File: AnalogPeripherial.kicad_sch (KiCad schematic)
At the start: 52 parts, among them J1 USART, J2 SWD, J3 USB_B_Mini, SW1 record, SW2 replay, SW3 SW_Nidec_CAS-120A1, U1 LD1117S33TR_SOT223, U2 STM32F373CCTx, U3 LM386, U5 TLV9061xDBV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

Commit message: PCB design still in progress
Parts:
- added C23: 33p, Capacitor_SMD:C_0805_2012Metric_Pad1.18x1.45mm_HandSolder, symbol Device:C
- added C24: 10u, Capacitor_SMD:C_0805_2012Metric_Pad1.18x1.45mm_HandSolder, symbol Device:C
- C16: value 100p -> 100u
- C17: value 0.047u -> 0.05u
- C18: value 470u -> 250u
- C19: value 330n -> 68n
- C20: value 47u -> 40u
- C21: value 120p -> 995p
- C22: value 3.3u -> 150n
- R11: value 10k -> 100
- R6: value 5.9k -> 2.2k
- R7, R8: value 200k -> 100k
- R9: value 787 -> 78.7
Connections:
- net 3V3: now also U2.1 (VBAT), U2.17 (VDD), U2.48 (VDD)
- net 3VA3: now also U2.24 (VDDSD), U2.9 (VDDA)
- net ADC1_IN1: now also R11.1; no longer R11.2
- net DAC1_OUT1: now also C24.1; no longer RV1.1
- net GND: now also C22.1, C23.1; no longer R11.1, U2.1 (VBAT), U2.17 (VDD), U2.24 (VDDSD), U2.48 (VDD), U2.9 (VDDA)
- net SPI1_NSS: now also U2.21 (PE8); no longer U2.38 (PA15)
- net at C21.2, R10.2, U5.1: now also R11.2; no longer C22.1
- net at C19.1, MK1.2 (+), R6.2: now also C23.2
- net NRST: no longer names the net of C1.1, U2.7 (NRST)
- new net: C24.2, RV1.1
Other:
- moved on the sheet: C1, C11, C12, C13, C14, C2, C4, C5, C7, C8, C9, D1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

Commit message: Finished model of PCB
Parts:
- removed U4: ~, my_custom_stuff:microSD, symbol my_custom_stuff:microSD
- added H1, H2, H3, H4: MountingHole, MountingHole:MountingHole_2.2mm_M2, symbol Mechanical:MountingHole
- added U4: ~, project:microSD, symbol project:SD_Card
- SW1, SW2: footprint my_custom_stuff:button -> project:button
- U3: footprint ADL5370ACPZ:M08A_TEX -> Package_SO:PowerIntegrations_SO-8
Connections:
- net 3V3: now also U4.4 (VDD); no longer R6.1, R7.1, U5.5 (V+)
- net 3VA3: now also R6.1, R7.1, U5.5 (V+)
- net GND: now also J3.6 (Shield), U4.12 (GND), U4.13 (GND), U4.14 (GND), U4.15 (GND), U4.6 (VSS)
- net PUSH_REC: now also U2.3 (PC14); no longer U2.19 (PB1)
- net PUSH_REPLAY: now also U2.2 (PC13); no longer U2.20 (PB2)
- net SPI1_MISO: now also U4.7 (DAT0)
- net SPI1_MOSI: now also U4.3 (CMD)
- net SPI1_NSS: now also U4.2 (CD)
- net SPI1_SCK: now also U4.5 (CLK)
- net SWCLK: now also J2.2 (Pin_2); no longer J2.3 (Pin_3)
- net SWDIO: now also J2.3 (Pin_3); no longer J2.2 (Pin_2)
- no-connect marks 26 -> 25
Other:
- moved on the sheet: C15, C16, C17, C18, C24, D2, D3, J1, J2, LS1, R3, R4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

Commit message: Order all files and folders
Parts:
- C18: value 250u -> 100u
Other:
- note added: "additional"
- note added: "ideally 250u"
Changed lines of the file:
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@@
 		)
 	)
+	(text "additional\n"
+		(exclude_from_sim no)
+		(at 221.488 123.952 0)
+		(effects
+			(font
+				(size 1.27 1.27)
+			)
+		)
+	)
 	(text "Power supply"
 		(exclude_from_sim no)
@@
 		)
 	)
+	(text "ideally 250u\n"
+		(exclude_from_sim no)
+		(at 247.396 92.456 0)
+		(effects
+			(font
+				(size 1.27 1.27)
+			)
+		)
+	)
 	(global_label "SWCLK"
 		(shape input)
@@
 		)
 		(instances
-			(project ""
+			(project "AnalogPeripherial"
 				(path "/0b175dd1-a91a-485c-9ff0-418ddbedb12c"
 					(reference "H1")
@@
 			)
 		)
-		(property "Value" "250u"
+		(property "Value" "100u"
 			(at 247.65 97.79 90)
 			(effects
@@
 		)
 		(instances
-			(project ""
+			(project "AnalogPeripherial"
 				(path "/0b175dd1-a91a-485c-9ff0-418ddbedb12c"
 					(reference "U4")

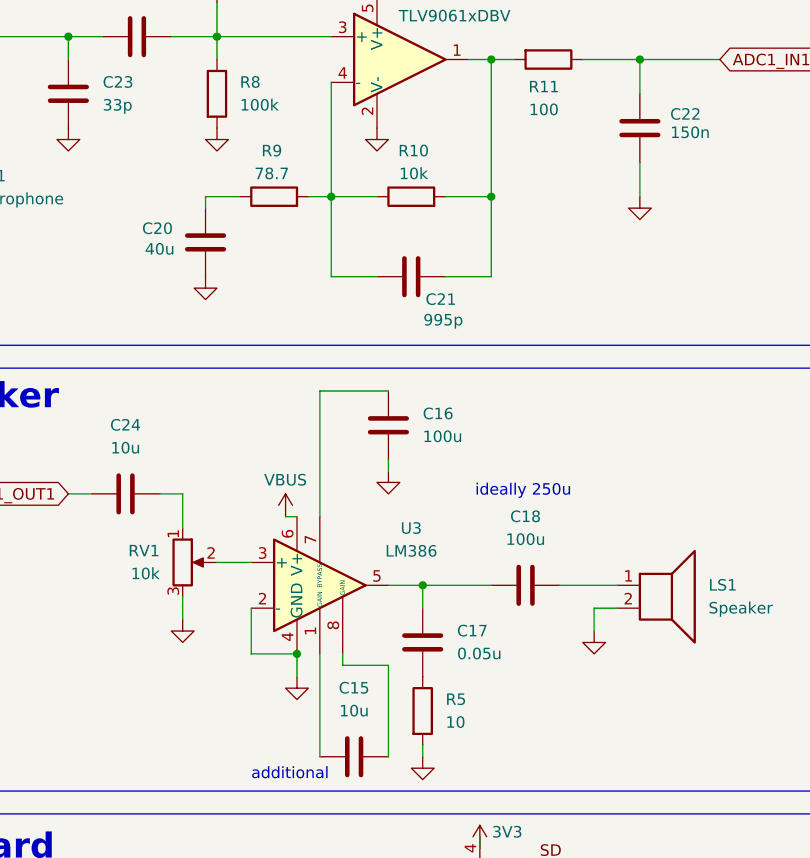
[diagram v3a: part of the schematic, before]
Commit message: Small changes in values of components
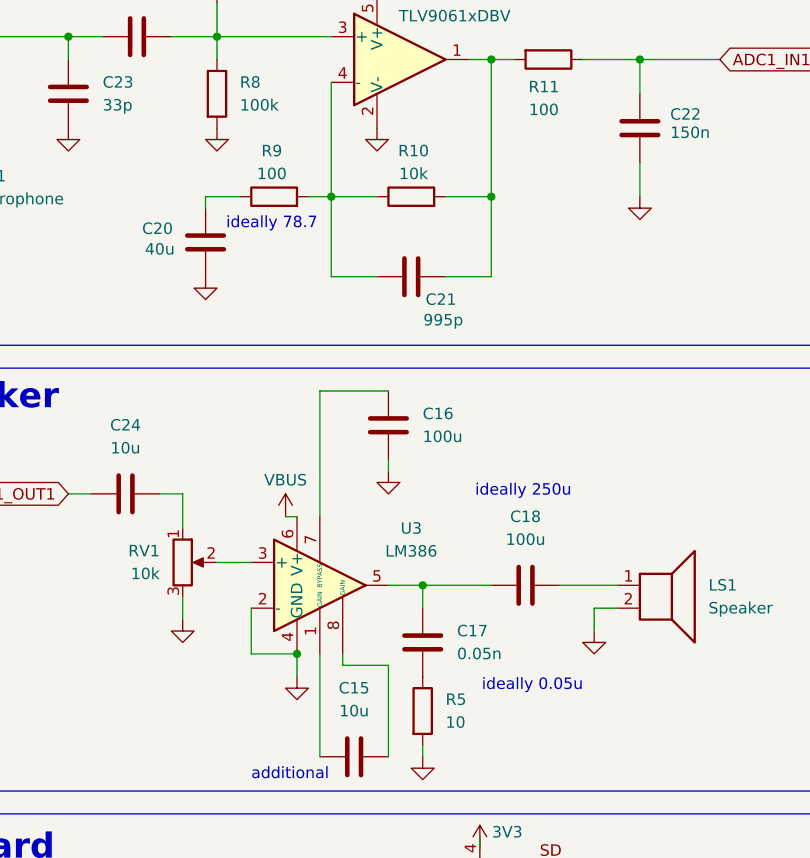
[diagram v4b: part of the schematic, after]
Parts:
- C17: value 0.05u -> 0.05n
- R9: value 78.7 -> 100
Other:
- note added: "ideally 0.05u"
- note added: "ideally 78.7"
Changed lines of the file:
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@@
 		)
 	)
+	(text "ideally 78.7"
+		(exclude_from_sim no)
+		(at 219.456 62.738 0)
+		(effects
+			(font
+				(size 1.27 1.27)
+			)
+		)
+	)
+	(text "ideally 0.05u\n"
+		(exclude_from_sim no)
+		(at 248.412 114.046 0)
+		(effects
+			(font
+				(size 1.27 1.27)
+			)
+		)
+	)
 	(global_label "SWCLK"
 		(shape input)
@@
 			)
 		)
-		(property "Value" "0.05u"
+		(property "Value" "0.05n"
 			(at 240.03 110.4899 0)
 			(effects
@@
 			)
 		)
-		(property "Value" "78.7"
+		(property "Value" "100"
 			(at 219.456 57.15 90)
 			(effects

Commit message: Start working on code
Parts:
- C20: value 40u -> 47u
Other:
- note added: "ideally 40u"
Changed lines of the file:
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@@
 	(wire
 		(pts
-			(xy 90.17 121.92) (xy 96.52 121.92)
-		)
-		(stroke
-			(width 0)
-			(type default)
-		)
-	)
-	(wire
-		(pts
 			(xy 217.17 105.41) (xy 217.17 110.49)
 		)
@@
 	(wire
 		(pts
-			(xy 45.72 137.16) (xy 49.53 137.16)
-		)
-		(stroke
-			(width 0)
-			(type default)
-		)
-	)
-	(wire
-		(pts
 			(xy 218.44 151.13) (xy 229.87 151.13)
 		)
@@
 	(wire
 		(pts
-			(xy 44.45 127) (xy 49.53 127)
-		)
-		(stroke
-			(width 0)
-			(type default)
-		)
-	)
-	(wire
-		(pts
 			(xy 69.85 100.33) (xy 69.85 101.6)
 		)
@@
 	(wire
 		(pts
-			(xy 90.17 124.46) (xy 96.52 124.46)
-		)
-		(stroke
-			(width 0)
-			(type default)
-		)
-	)
-	(wire
-		(pts
 			(xy 83.82 100.33) (xy 96.52 100.33)
 		)
@@
 	(wire
 		(pts
-			(xy 90.17 111.76) (xy 96.52 111.76)
-		)
-		(stroke
-			(width 0)
-			(type default)
-		)
-	)
-	(wire
-		(pts
 			(xy 162.56 166.37) (xy 160.02 166.37)
 		)
@@
 	(wire
 		(pts
-			(xy 90.17 142.24) (xy 96.52 142.24)
-		)
-		(stroke
-			(width 0)
-			(type default)
-		)
-	)
-	(wire
-		(pts
 			(xy 107.95 100.33) (xy 118.11 100.33)
 		)
@@
 	(wire
 		(pts
-			(xy 44.45 124.46) (xy 49.53 124.46)
-		)
-		(stroke
-			(width 0)
-			(type default)
-		)
-	)
-	(wire
-		(pts
 			(xy 83.82 88.9) (xy 83.82 90.17)
 		)
@@
 	(wire
 		(pts
-			(xy 90.17 134.62) (xy 96.52 134.62)
-		)
-		(stroke
-			(width 0)
-			(type default)
-		)
-	)
-	(wire
-		(pts
 			(xy 74.93 101.6) (xy 74.93 100.33)
 		)
@@
 	(wire
 		(pts
-			(xy 90.17 129.54) (xy 96.52 129.54)
-		)
-		(stroke
-			(width 0)
-			(type default)
-		)
-	)
-	(wire
-		(pts
 			(xy 208.28 41.91) (xy 213.36 41.91)
 		)
@@
 	(wire
 		(pts
-			(xy 43.18 114.3) (xy 49.53 114.3)
-		)
-		(stroke
-			(width 0)
-			(type default)
-		)
-	)
-	(wire
-		(pts
 			(xy 67.31 185.42) (xy 67.31 186.69)
 		)
@@
 	(wire
 		(pts
-			(xy 90.17 119.38) (xy 96.52 119.38)
-		)
-		(stroke
-			(width 0)
-			(type default)
-		)
-	)
-	(wire
-		(pts
 			(xy 67.31 186.69) (xy 67.31 187.96)
 		)
@@
 	(wire
 		(pts
-			(xy 90.17 149.86) (xy 96.52 149.86)
+			(xy 90.17 149.86) (xy 91.44 149.86)
 		)
 		(stroke
@@
 	(wire
 		(pts
-			(xy 90.17 139.7) (xy 96.52 139.7)
-		)
-		(stroke
-			(width 0)
-			(type default)
-		)
-	)
-	(wire
-		(pts
 			(xy 22.86 119.38) (xy 22.86 118.11)
 		)
@@
 	(wire
 		(pts
-			(xy 90.17 137.16) (xy 96.52 137.16)
-		)
-		(stroke
-			(width 0)
-			(type default)
-		)
-	)
-	(wire
-		(pts
 			(xy 106.68 72.39) (xy 106.68 71.12)
 		)
@@
 	(wire
 		(pts
-			(xy 90.17 132.08) (xy 96.52 132.08)
-		)
-		(stroke
-			(width 0)
-			(type default)
-		)
-	)
-	(wire
-		(pts
 			(xy 88.9 38.1) (xy 88.9 40.64)
 		)
@@
 		)
 	)
+	(text "ideally 40u"
+		(exclude_from_sim no)
+		(at 203.2 68.072 0)
+		(effects
+			(font
+				(size 1.27 1.27)
+			)
+		)
+	)
 	(text "ideally 250u\n"
 		(exclude_from_sim no)
@@
 	(global_label "SPI1_MOSI"
 		(shape input)
-		(at 96.52 149.86 0)
+		(at 91.44 149.86 0)
 		(fields_autoplaced yes)
 		(effects
@@
 		)
 		(property "Intersheetrefs" "${INTERSHEET_REFS}"
-			(at 109.3628 149.86 0)
+			(at 104.2828 149.86 0)
 			(effects
 				(font
@@
 	(global_label "ADC1_IN1"
 		(shape input)
-		(at 96.52 111.76 0)
+		(at 90.17 111.76 0)
 		(fields_autoplaced yes)
 		(effects
@@
 		)
 		(property "Intersheetrefs" "${INTERSHEET_REFS}"
-			(at 108.4557 111.76 0)
+			(at 102.1057 111.76 0)
 			(effects
 				(font
@@
 	(global_label "HSE_OUT"
 		(shape input)
-		(at 44.45 127 180)
+		(at 49.53 127 180)
 		(fields_autoplaced yes)
 		(effects
@@
 		)
 		(property "Intersheetrefs" "${INTERSHEET_REFS}"
-			(at 33.1796 127 0)
+			(at 38.2596 127 0)
 			(effects
 				(font
@@
 	(global_label "USART1_TX"
 		(shape input)
-		(at 96.52 129.54 0)
+		(at 90.17 129.54 0)
 		(fields_autoplaced yes)
 		(effects
@@
 		)
 		(property "Intersheetrefs" "${INTERSHEET_REFS}"
-			(at 109.7256 129.54 0)
+			(at 103.3756 129.54 0)
 			(effects
 				(font
@@
 	(global_label "SPI1_NSS"
 		(shape input)
-		(at 45.72 137.16 180)
+		(at 49.53 137.16 180)
 		(fields_autoplaced yes)
 		(effects
@@
 		)
 		(property "Intersheetrefs" "${INTERSHEET_REFS}"
-			(at 33.7239 137.16 0)
+			(at 37.5339 137.16 0)
 			(effects
 				(font
@@
 	(global_label "HSE_IN"
 		(shape input)
-		(at 44.45 124.46 180)
+		(at 49.53 124.46 180)
 		(fields_autoplaced yes)
 		(effects
@@
 		)
 		(property "Intersheetrefs" "${INTERSHEET_REFS}"
-			(at 34.8729 124.46 0)
+			(at 39.9529 124.46 0)
 			(effects
 				(font
@@
 	(global_label "SWCLK"
 		(shape input)
-		(at 96.52 142.24 0)
+		(at 90.17 142.24 0)
 		(fields_autoplaced yes)
 		(effects
@@
 		)
 		(property "Intersheetrefs" "${INTERSHEET_REFS}"
-			(at 105.7342 142.24 0)
+			(at 99.3842 142.24 0)
 			(effects
 				(font
@@
 	(global_label "SPI1_MISO"
 		(shape input)
-		(at 96.52 124.46 0)
+		(at 90.17 124.46 0)
 		(fields_autoplaced yes)
 		(effects
@@
 		)
 		(property "Intersheetrefs" "${INTERSHEET_REFS}"
-			(at 109.3628 124.46 0)
+			(at 103.0128 124.46 0)
 			(effects
 				(font
@@
 	(global_label "USB-"
 		(shape input)
-		(at 96.52 134.62 0)
+		(at 90.17 134.62 0)
 		(fields_autoplaced yes)
 		(effects
@@
 		)
 		(property "Intersheetrefs" "${INTERSHEET_REFS}"
-			(at 104.8876 134.62 0)
+			(at 98.5376 134.62 0)
 			(effects
 				(font
@@
 	(global_label "USART1_RX"
 		(shape input)
-		(at 96.52 132.08 0)
+		(at 90.17 132.08 0)
 		(fields_autoplaced yes)
 		(effects
@@
 		)
 		(property "Intersheetrefs" "${INTERSHEET_REFS}"
-			(at 110.028 132.08 0)
+			(at 103.678 132.08 0)
 			(effects
 				(font
@@
 	(global_label "DAC1_OUT1"
 		(shape input)
-		(at 96.52 119.38 0)
+		(at 90.17 119.38 0)
 		(fields_autoplaced yes)
 		(effects
@@
 		)
 		(property "Intersheetrefs" "${INTERSHEET_REFS}"
-			(at 110.149 119.38 0)
+			(at 103.799 119.38 0)
 			(effects
 				(font
@@
 	(global_label "SPI1_SCK"
 		(shape input)
-		(at 96.52 121.92 0)
+		(at 90.17 121.92 0)
 		(fields_autoplaced yes)
 		(effects
@@
 		)
 		(property "Intersheetrefs" "${INTERSHEET_REFS}"
-			(at 108.5161 121.92 0)
+			(at 102.1661 121.92 0)
 			(effects
 				(font
@@
 	(global_label "USB+"
 		(shape input)
-		(at 96.52 137.16 0)
+		(at 90.17 137.16 0)
 		(fields_autoplaced yes)
 		(effects
@@
 		)
 		(property "Intersheetrefs" "${INTERSHEET_REFS}"
-			(at 104.8876 137.16 0)
+			(at 98.5376 137.16 0)
 			(effects
 				(font
@@
 	(global_label "BOOT0"
 		(shape input)
-		(at 43.18 114.3 180)
+		(at 49.53 114.3 180)
 		(fields_autoplaced yes)
 		(effects
@@
 		)
 		(property "Intersheetrefs" "${INTERSHEET_REFS}"
-			(at 34.0867 114.3 0)
+			(at 40.4367 114.3 0)
 			(effects
 				(font
@@
 	(global_label "SWDIO"
 		(shape input)
-		(at 96.52 139.7 0)
+		(at 90.17 139.7 0)
 		(fields_autoplaced yes)
 		(effects
@@
 		)
 		(property "Intersheetrefs" "${INTERSHEET_REFS}"
-			(at 105.3714 139.7 0)
+			(at 99.0214 139.7 0)
 			(effects
 				(font
@@
 			)
 		)
-		(property "Value" "40u"
+		(property "Value" "47u"
 			(at 207.01 65.532 0)
 			(effects
